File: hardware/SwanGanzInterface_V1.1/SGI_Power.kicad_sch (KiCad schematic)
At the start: 24 parts, among them J1 Conn_01x02_Pin, Q1 SQ2389CES-T1_GE3, SW1 Power_Switch, U1 LM2937ET-3.3_NOPB, U14 OPA2350, U2 LM4041CILPR, U3 OPA2350

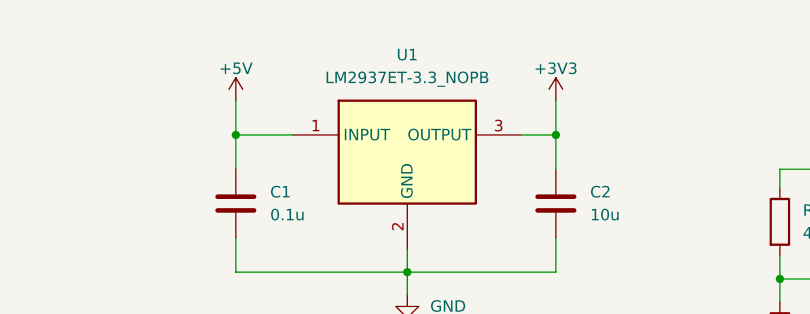
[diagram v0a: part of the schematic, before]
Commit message: LCD spi debugging pins
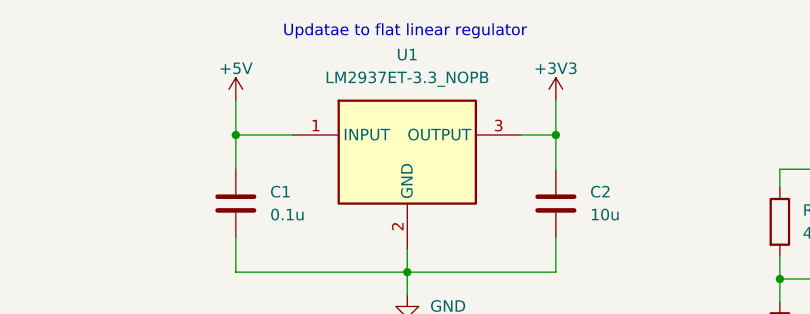
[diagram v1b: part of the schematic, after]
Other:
- note added: "Updatae to flat linear regulator"
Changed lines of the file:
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@@
+		)
+	)
+	(text "Updatae to flat linear regulator"
+		(exclude_from_sim no)
+		(at 105.156 17.78 0)
+		(effects
+			(font
+				(size 1.27 1.27)
+			)
 		)
 	)

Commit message: Schematic Check
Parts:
- removed U1: LM2937ET-3.3_NOPB, SGI_FootprintsLib:TO254P470X1028X1955-3P, symbol SGI_SymbolLib:LM2937ET-3.3_NOPB
- added IC1: LM2937ESX-3.3_NOPB, SGI_FootprintsLib:LM2937ESX-3.3_NOPB, symbol SGI_SymbolLib:LM2937ESX-3.3_NOPB
- renumbered C28 to C4, R3 to R1, R4 to R2, R5 to R3, TP3 to TP1, TP1 to TP2, TP2 to TP3, U2 to U1, U3 to U2, U14 to U3
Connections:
- net +3V3: now also IC1.3 (OUTPUT)
- net +5V: now also IC1.1 (INPUT)
- net GND: now also IC1.2 (GND), IC1.4 (TAB)
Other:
- note added: "Linear Regulator"
- note added: "Optional Battery Connection"
- note added: "Power Sheet"
- note added: "Power Switch and Reverse Polarity Protection"
- note added: "Voltage Followers for Analog Circuits"
- note removed: "Maybe Switch Part Numbers"
- moved on the sheet: C1, C2, C3, C4, H1, H2, H3, H4, J1, Q1, R1, R2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

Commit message: Filter paramaters and assigned footprints
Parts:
- J1: footprint (none) -> Connector_PinHeader_2.54mm:PinHeader_1x02_P2.54mm_Vertical
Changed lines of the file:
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@@
 			)
 		)
-		(property "Footprint" ""
+		(property "Footprint" "Connector_PinHeader_2.54mm:PinHeader_1x02_P2.54mm_Vertical"
 			(at 28.956 179.578 0)
 			(effects
